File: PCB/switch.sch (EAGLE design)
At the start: 2 parts

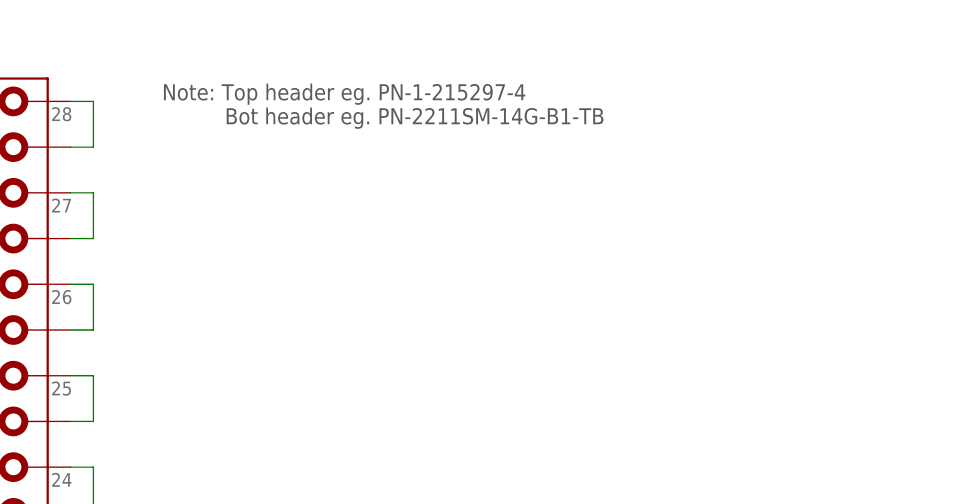
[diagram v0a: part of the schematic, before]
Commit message: feat: add header package ontline
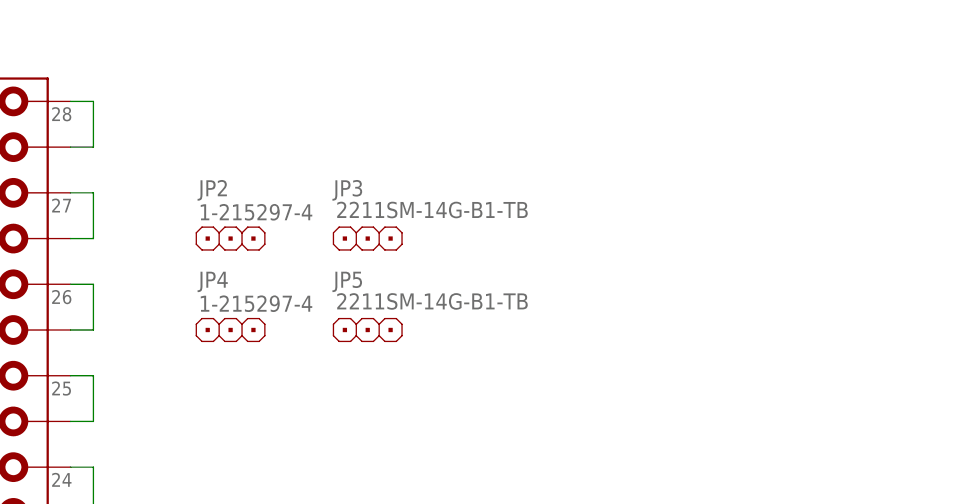
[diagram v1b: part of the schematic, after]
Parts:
- added JP2, JP4: 1-215297-4, pinhead:1X3
- added JP3, JP5: 2211SM-14G-B1-TB, pinhead:1X3
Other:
- note removed: "Note: Top header eg. PN-1-215297-4 Bot header eg. PN-2211SM-14G-B1-TB"
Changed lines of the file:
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@@
 <part name="FRAME1" library="frames" deviceset="A4L-LOC" device=""/>
 <part name="S1" library="switch" deviceset="TL32WO" device="" value="7101MD9AQE"/>
+<part name="JP2" library="pinhead" deviceset="1X3" device="" value="1-215297-4"/>
+<part name="JP3" library="pinhead" deviceset="1X3" device="" value="2211SM-14G-B1-TB"/>
+<part name="JP4" library="pinhead" deviceset="1X3" device="" value="1-215297-4"/>
+<part name="JP5" library="pinhead" deviceset="1X3" device="" value="2211SM-14G-B1-TB"/>
 </parts>
 <sheets>
 <sheet>
 <plain>
-<text x="109.22" y="157.48" size="1.778" layer="97">Note: Top header eg. PN-1-215297-4
-          Bot header eg. PN-2211SM-14G-B1-TB		</text>
 <text x="213.36" y="20.32" size="2.54" layer="94" font="vector" ratio="15">StavJi</text>
 </plain>
@@
 <attribute name="VALUE" x="114.3" y="42.672" size="1.778" layer="96"/>
 </instance>
+<instance part="JP2" gate="G$1" x="116.84" y="144.78" smashed="yes">
+<attribute name="NAME" x="113.284" y="149.479" size="1.778" layer="95"/>
+<attribute name="VALUE" x="113.284" y="146.812" size="1.778" layer="96"/>
+</instance>
+<instance part="JP3" gate="G$1" x="132.08" y="144.78" smashed="yes">
+<attribute name="NAME" x="128.27" y="149.479" size="1.778" layer="95"/>
+<attribute name="VALUE" x="128.524" y="147.066" size="1.778" layer="96"/>
+</instance>
+<instance part="JP4" gate="G$1" x="116.84" y="134.62" smashed="yes">
+<attribute name="NAME" x="113.284" y="139.319" size="1.778" layer="95"/>
+<attribute name="VALUE" x="113.284" y="136.652" size="1.778" layer="96"/>
+</instance>
+<instance part="JP5" gate="G$1" x="132.08" y="134.62" smashed="yes">
+<attribute name="NAME" x="128.27" y="139.319" size="1.778" layer="95"/>
+<attribute name="VALUE" x="128.524" y="136.906" size="1.778" layer="96"/>
+</instance>
 </instances>
 <busses>
@@
 </schematic>
 </drawing>
-<compatibility>
-<note version="6.3" minversion="6.2.2" severity="warning">
-Since Version 6.2.2 text objects can contain more than one line,
-which will not be processed correctly with this version.
-</note>
-</compatibility>
 </eagle>

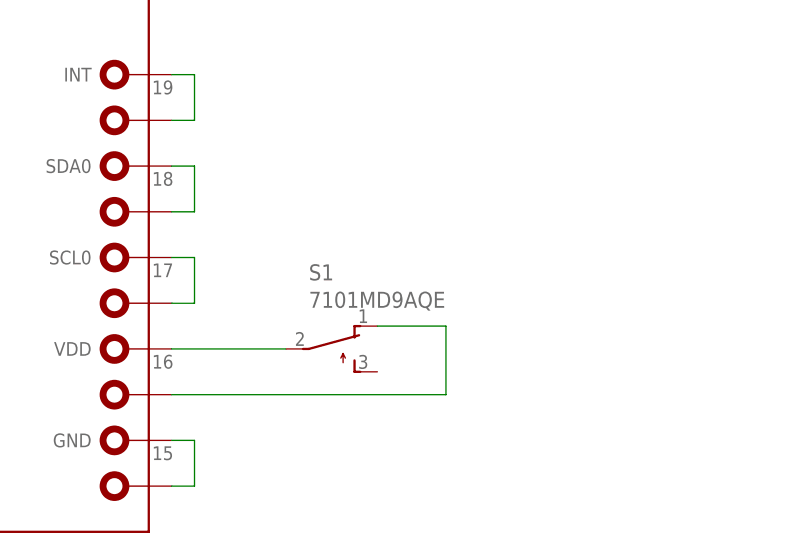
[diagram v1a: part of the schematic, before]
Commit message: fix: switch package ontline
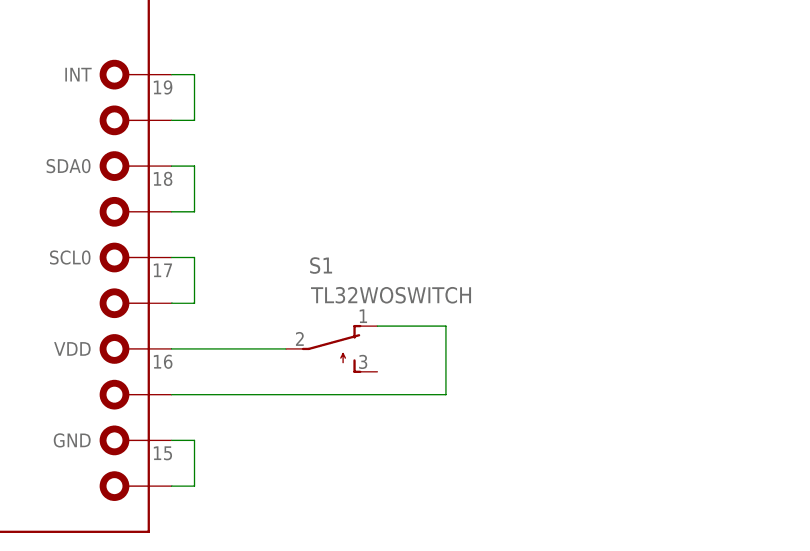
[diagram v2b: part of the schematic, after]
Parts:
- S1: value 7101MD9AQE -> TL32WOSWITCH; device switch:TL32WO -> switch:TL32WOSWITCH
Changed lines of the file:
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@@
 <part name="JP1" library="bigclown" deviceset="BC-MODULE-CORE-TOP-BOT" device="" value="BC-MODULE-CORE"/>
 <part name="FRAME1" library="frames" deviceset="A4L-LOC" device=""/>
-<part name="S1" library="switch" deviceset="TL32WO" device="" value="7101MD9AQE"/>
 <part name="JP2" library="pinhead" deviceset="1X3" device="" value="1-215297-4"/>
 <part name="JP3" library="pinhead" deviceset="1X3" device="" value="2211SM-14G-B1-TB"/>
 <part name="JP4" library="pinhead" deviceset="1X3" device="" value="1-215297-4"/>
 <part name="JP5" library="pinhead" deviceset="1X3" device="" value="2211SM-14G-B1-TB"/>
+<part name="S1" library="switch" deviceset="TL32WO" device="SWITCH"/>
 </parts>
 <sheets>
@@
 </instance>
 <instance part="FRAME1" gate="G$1" x="0" y="0"/>
-<instance part="S1" gate="BEF1" x="116.84" y="38.1" smashed="yes" rot="R270">
-<attribute name="NAME" x="114.3" y="45.72" size="1.778" layer="95"/>
-<attribute name="VALUE" x="114.3" y="42.672" size="1.778" layer="96"/>
-</instance>
 <instance part="JP2" gate="G$1" x="116.84" y="144.78" smashed="yes">
 <attribute name="NAME" x="113.284" y="149.479" size="1.778" layer="95"/>
@@
 <attribute name="VALUE" x="128.524" y="136.906" size="1.778" layer="96"/>
 </instance>
+<instance part="S1" gate="BEF1" x="116.84" y="38.1" smashed="yes" rot="R270">
+<attribute name="NAME" x="114.3" y="46.482" size="1.778" layer="95"/>
+<attribute name="VALUE" x="114.554" y="43.18" size="1.778" layer="96"/>
+</instance>
 </instances>
